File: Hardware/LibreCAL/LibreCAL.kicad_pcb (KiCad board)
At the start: 4 copper layers, 55 x 73.5 mm, 132 parts, among them J1 901-10510-2, J2 901-10510-2, J3 901-10510-2, J4 901-10510-2, J5 USB_C_Receptacle_USB2.0, J6 TC2030-ARM, Q1 IRLML2060, SW1 TL3301NF160QG, SW2 TL3301CF160QG, SW3 TL3301CF160QG, U1 PE426462, U10 W25N01GVZEIG, U2 PE426462, U3 PE426462, U4 PE426462, U5 W25Q16JVSNIQ, U6 IP4234CZ6, U7 RP2040, U9 MIC5528-3.3YMT-TR, Y1 ECS-120-8-36-CKM-TR3

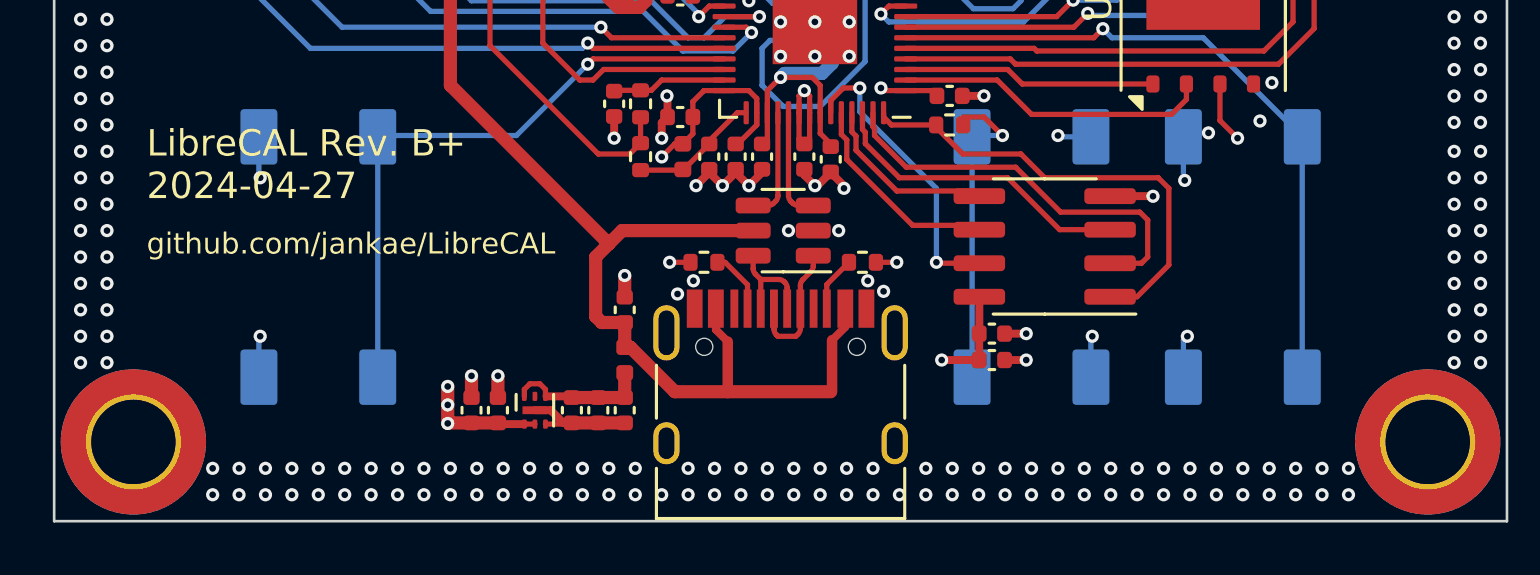
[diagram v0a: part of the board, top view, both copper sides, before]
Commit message: wip: add 1gbit flash
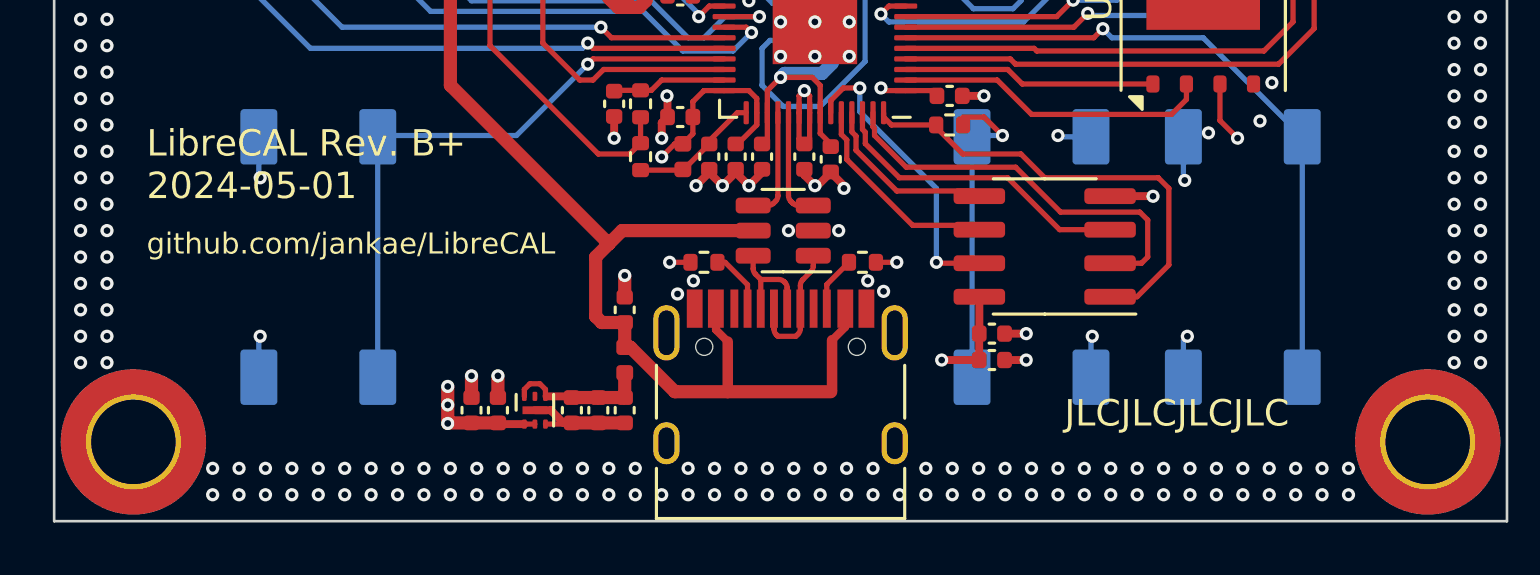
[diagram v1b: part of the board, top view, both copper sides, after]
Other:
- board text added: "JLCJLCJLCJLC"
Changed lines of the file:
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@@
 	(title_block
 		(title "LibreCAL")
-		(date "2024-04-27")
+		(date "2024-05-01")
 		(rev "B+")
 	)
@@
 		)
 	)
+	(gr_text "JLCJLCJLCJLC"
+		(at 138.25 136 0)
+		(layer "F.SilkS")
+		(effects
+			(font
+				(size 1 1)
+				(thickness 0.15)
+			)
+			(justify left bottom)
+		)
+	)
